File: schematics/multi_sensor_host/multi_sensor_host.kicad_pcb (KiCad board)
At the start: 2 copper layers, 70 x 146 mm, 173 parts, among them J1 left hand 0, J10 swd, J11 stm_boot, J13 right hand 0, J14 right hand 1, J15 right hand 2, J16 right hand 3, J17 rst, J18 left hand 3, J19 left leg 0, J2 left hand 1, J20 left leg 1, J21 right lef 0, J22 right leg 1, J23 torso 0, J24 torso 1, J25 torso 2, J26 torso 3, J3 bm_cfg, J4 left hand 2, J5 tx, J6 MY_USB_B, J8 rx, J9 uart1, U1 TCA9548A_TSSOP, U11 MCP111, U12 BM71BLES1FC2-0B02AA, U2 TCA9548A_TSSOP, U3 74HC165, U4 74HC165, U5 74HC165, U6 74HC165, U8 MCP73812, U9 MCP1603, Y1 Crystal

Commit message: Probably good enough...
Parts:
- moved J9 0.11 mm to (72.1, 129.1)
- moved C31 0.10 mm to (71.9, 124.4)
- moved R93 0.10 mm to (74.9, 130.4)
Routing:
- net VDD: track 1108.4 -> 1096.4 mm
- net /rst: track 153.4 -> 155.3 mm
- net /stm_rx: track 78.6 -> 79.5 mm
- net /stm_tx: track 86.3 -> 87.2 mm

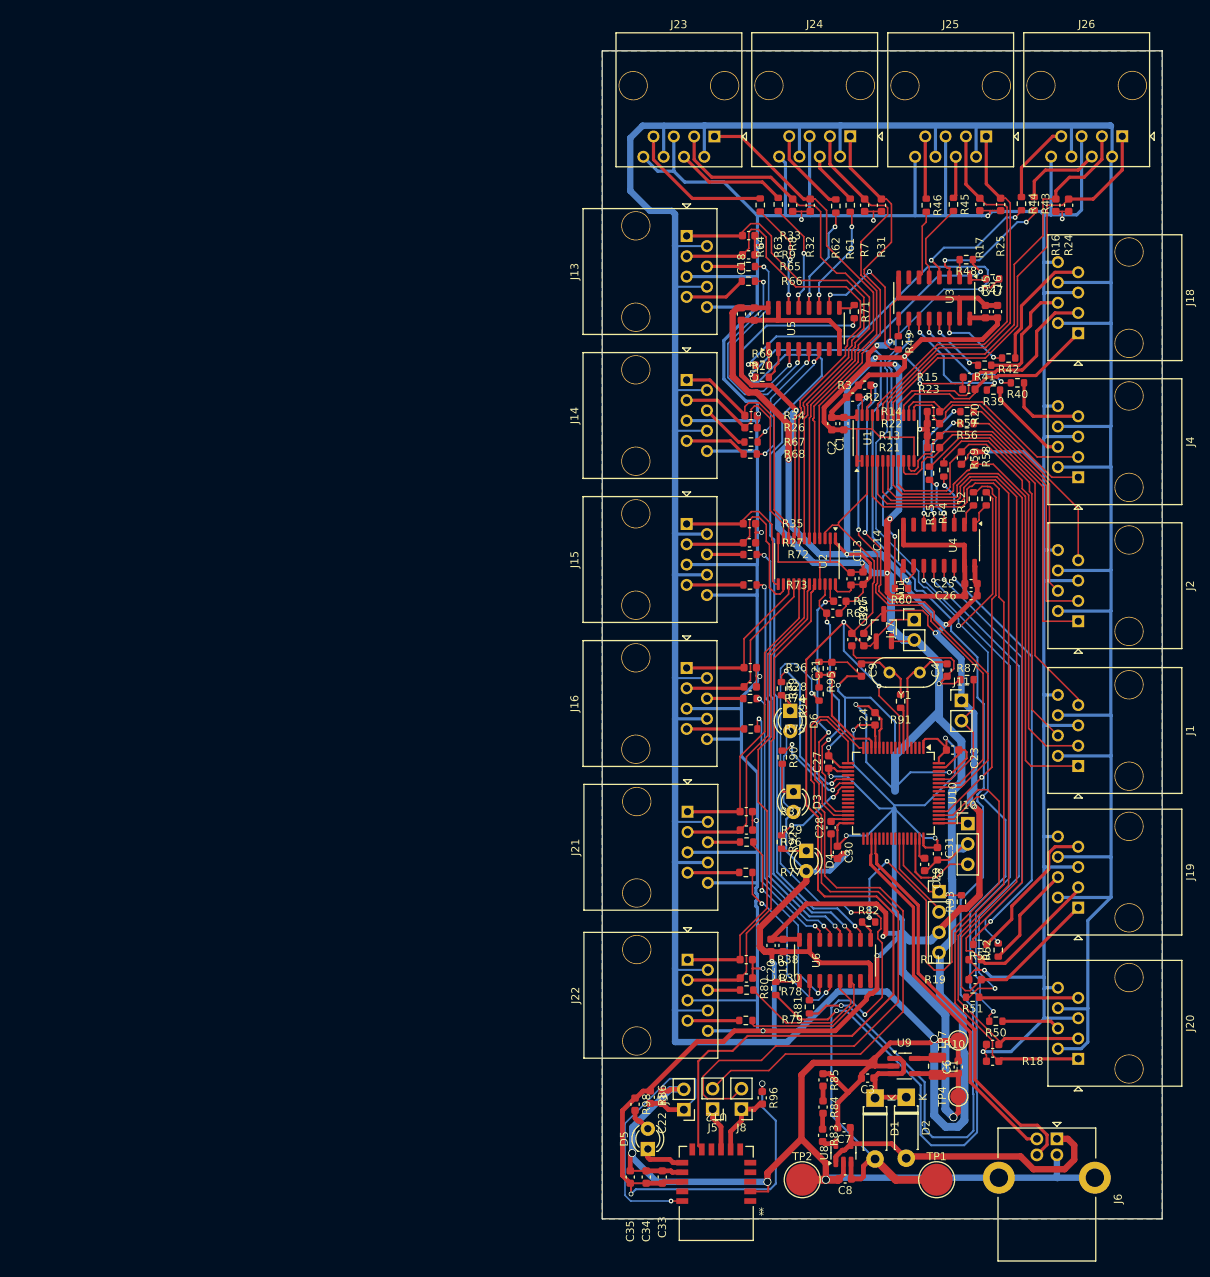
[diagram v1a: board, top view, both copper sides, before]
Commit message: Removing old wires.
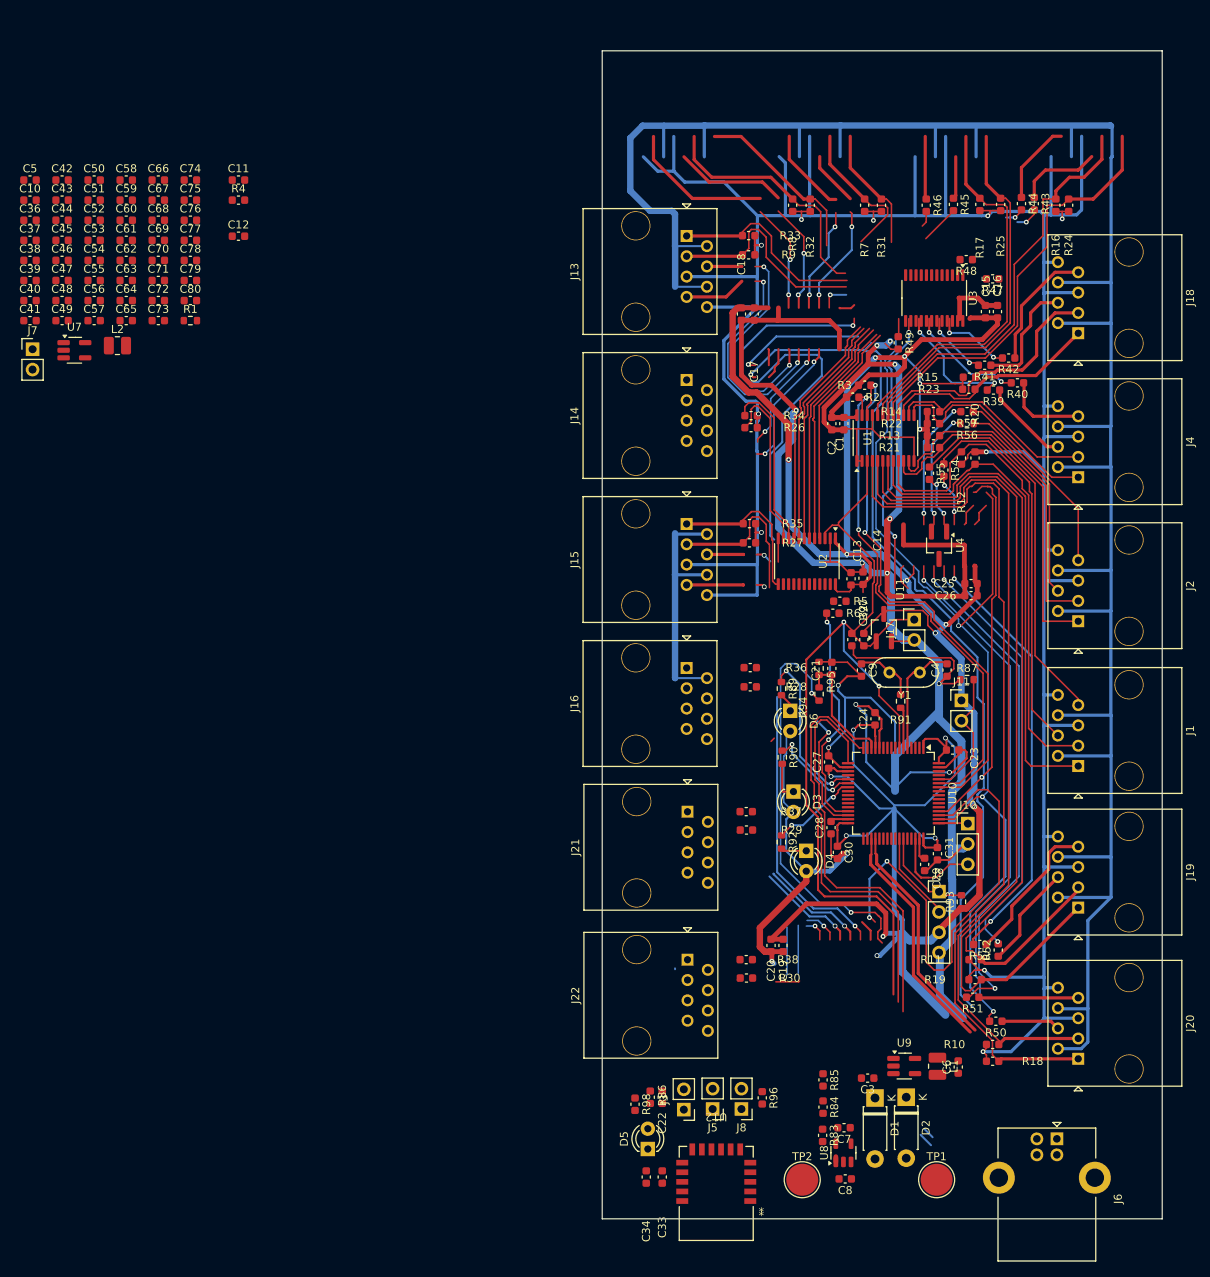
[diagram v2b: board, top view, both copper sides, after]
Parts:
- removed C35: 4u7, Capacitor_SMD:C_0603_1608Metric
- removed J23: torso 0, Connector_RJ:RJ45_OST_PJ012-8P8CX_Vertical
- removed J24: torso 1, Connector_RJ:RJ45_OST_PJ012-8P8CX_Vertical
- removed J25: torso 2, Connector_RJ:RJ45_OST_PJ012-8P8CX_Vertical
- removed J26: torso 3, Connector_RJ:RJ45_OST_PJ012-8P8CX_Vertical
- removed R58, R59, R60, R61, R62, R63, R64, R65, R66, R67, R68, R69, R70, R71, R72, R73, R74, R75, R76, R77, R78, R79, R80, R81, R82: 2k, Resistor_SMD:R_0603_1608Metric
- removed TP4: Vdd, TestPoint:TestPoint_Pad_D2.0mm
- removed TP7: gnd, TestPoint:TestPoint_Pad_D2.0mm
- removed U5, U6: 74HC165, Package_SO:SO-16_3.9x9.9mm_P1.27mm
- added C10: 22u, Capacitor_SMD:C_0603_1608Metric, F.Cu at (-41.5, 42.7)
- added C11: 100n, Capacitor_SMD:C_0603_1608Metric, F.Cu at (-15.5, 40.1)
- added C12: 22u, Capacitor_SMD:C_0603_1608Metric, F.Cu at (-15.5, 47.2)
- added C36: 4u7, Capacitor_SMD:C_0603_1608Metric, F.Cu at (-41.5, 45.2)
- added C37: 100n, Capacitor_SMD:C_0603_1608Metric, F.Cu at (-41.5, 47.7)
- added C38: 4u7, Capacitor_SMD:C_0603_1608Metric, F.Cu at (-41.5, 50.2)
- added C39: 100n, Capacitor_SMD:C_0603_1608Metric, F.Cu at (-41.5, 52.7)
- added C40: 4u7, Capacitor_SMD:C_0603_1608Metric, F.Cu at (-41.5, 55.2)
- added C41: 100n, Capacitor_SMD:C_0603_1608Metric, F.Cu at (-41.5, 57.7)
- added C42: 4u7, Capacitor_SMD:C_0603_1608Metric, F.Cu at (-37.5, 40.1)
- added C43: 100n, Capacitor_SMD:C_0603_1608Metric, F.Cu at (-37.5, 42.7)
- added C44: 4u7, Capacitor_SMD:C_0603_1608Metric, F.Cu at (-37.5, 45.2)
- added C45: 100n, Capacitor_SMD:C_0603_1608Metric, F.Cu at (-37.5, 47.7)
- added C46: 4u7, Capacitor_SMD:C_0603_1608Metric, F.Cu at (-37.5, 50.2)
- added C47: 100n, Capacitor_SMD:C_0603_1608Metric, F.Cu at (-37.5, 52.7)
- added C48: 4u7, Capacitor_SMD:C_0603_1608Metric, F.Cu at (-37.5, 55.2)
- added C49: 100n, Capacitor_SMD:C_0603_1608Metric, F.Cu at (-37.5, 57.7)
- added C5: 4u7, Capacitor_SMD:C_0603_1608Metric, F.Cu at (-41.5, 40.1)
- added C50: 4u7, Capacitor_SMD:C_0603_1608Metric, F.Cu at (-33.5, 40.1)
- added C51: 100n, Capacitor_SMD:C_0603_1608Metric, F.Cu at (-33.5, 42.7)
- added C52: 4u7, Capacitor_SMD:C_0603_1608Metric, F.Cu at (-33.5, 45.2)
- added C53: 100n, Capacitor_SMD:C_0603_1608Metric, F.Cu at (-33.5, 47.7)
- added C54: 4u7, Capacitor_SMD:C_0603_1608Metric, F.Cu at (-33.5, 50.2)
- added C55: 100n, Capacitor_SMD:C_0603_1608Metric, F.Cu at (-33.5, 52.7)
- added C56: 4u7, Capacitor_SMD:C_0603_1608Metric, F.Cu at (-33.5, 55.2)
- added C57: 100n, Capacitor_SMD:C_0603_1608Metric, F.Cu at (-33.5, 57.7)
- added C58: 4u7, Capacitor_SMD:C_0603_1608Metric, F.Cu at (-29.5, 40.1)
- added C59: 100n, Capacitor_SMD:C_0603_1608Metric, F.Cu at (-29.5, 42.7)
- added C60: 4u7, Capacitor_SMD:C_0603_1608Metric, F.Cu at (-29.5, 45.2)
- added C61: 100n, Capacitor_SMD:C_0603_1608Metric, F.Cu at (-29.5, 47.7)
- added C62: 4u7, Capacitor_SMD:C_0603_1608Metric, F.Cu at (-29.5, 50.2)
- added C63: 100n, Capacitor_SMD:C_0603_1608Metric, F.Cu at (-29.5, 52.7)
- added C64: 4u7, Capacitor_SMD:C_0603_1608Metric, F.Cu at (-29.5, 55.2)
- added C65: 100n, Capacitor_SMD:C_0603_1608Metric, F.Cu at (-29.5, 57.7)
- added C66: 4u7, Capacitor_SMD:C_0603_1608Metric, F.Cu at (-25.5, 40.1)
- added C67: 100n, Capacitor_SMD:C_0603_1608Metric, F.Cu at (-25.5, 42.7)
- added C68: 4u7, Capacitor_SMD:C_0603_1608Metric, F.Cu at (-25.5, 45.2)
- added C69: 100n, Capacitor_SMD:C_0603_1608Metric, F.Cu at (-25.5, 47.7)
- added C70: 4u7, Capacitor_SMD:C_0603_1608Metric, F.Cu at (-25.5, 50.2)
- added C71: 100n, Capacitor_SMD:C_0603_1608Metric, F.Cu at (-25.5, 52.7)
- added C72: 4u7, Capacitor_SMD:C_0603_1608Metric, F.Cu at (-25.5, 55.2)
- added C73: 100n, Capacitor_SMD:C_0603_1608Metric, F.Cu at (-25.5, 57.7)
- added C74: 4u7, Capacitor_SMD:C_0603_1608Metric, F.Cu at (-21.5, 40.1)
- added C75: 100n, Capacitor_SMD:C_0603_1608Metric, F.Cu at (-21.5, 42.7)
- added C76: 4u7, Capacitor_SMD:C_0603_1608Metric, F.Cu at (-21.5, 45.2)
- added C77: 100n, Capacitor_SMD:C_0603_1608Metric, F.Cu at (-21.5, 47.7)
- added C78: 4u7, Capacitor_SMD:C_0603_1608Metric, F.Cu at (-21.5, 50.2)
- added C79: 100n, Capacitor_SMD:C_0603_1608Metric, F.Cu at (-21.5, 52.7)
- added C80: 22u, Capacitor_SMD:C_0603_1608Metric, F.Cu at (-21.5, 55.2)
- added J7: rst_bm71, Connector_PinHeader_2.54mm:PinHeader_1x02_P2.54mm_Vertical, F.Cu at (-41.2, 61.3)
- added L2: 4.7uH, Inductor_SMD:L_1008_2520Metric, F.Cu at (-30.6, 60.9)
- added R1: 100k, Resistor_SMD:R_0603_1608Metric, F.Cu at (-21.5, 57.7)
- added R4: 2k, Capacitor_SMD:C_0603_1608Metric, F.Cu at (-15.5, 42.7)
- added U7: MCP1603, Package_TO_SOT_SMD:SOT-23-5_HandSoldering, F.Cu at (-36.0, 61.4)
- C14, C2, C33, C34, C6: value 4u7 -> 22u
- C15, C19, C25: value 100n -> 4u7
- C16, C18, C20, C26: value 4u7 -> 100n
- J17: value rst -> rst_mcu
- R39, R40, R41, R42, R43, R44, R45, R46, R47, R48, R49, R50, R51, R52, R53, R54, R55: footprint Resistor_SMD:R_0603_1608Metric -> Capacitor_SMD:C_0603_1608Metric
- R56: value 2k -> 100k
- R57: value 2k -> 10k; footprint Resistor_SMD:R_0603_1608Metric -> Capacitor_SMD:C_0603_1608Metric
- U3: value 74HC165 -> TCA9548A_TSSOP; footprint Package_SO:SO-16_3.9x9.9mm_P1.27mm -> Package_SO:TSSOP-24_4.4x7.8mm_P0.65mm
- U4: value 74HC165 -> MCP111; footprint Package_SO:SO-16_3.9x9.9mm_P1.27mm -> Package_TO_SOT_SMD:TSOT-23_HandSoldering
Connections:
- net /lh_scl_2 renamed /scl_4
- net /lh_sda_2 renamed /sda_4
- net /rh_scl_2 renamed /scl_12
- net /rh_sda_2 renamed /sda_12
- C15 pad 1: VDD -> /rst_bm71
- C16 pad 1: VDD -> VCC
- C18 pad 1: VDD -> VCC
- C32 pad 1: /rst -> /rst_mcu
- C33 pad 1: VDD -> VCC
- C34 pad 1: VDD -> VCC
- J1 pad 1: /lh_sda_0 -> /sda_0
- J1 pad 3: /lh_scl_0 -> /scl_0
- J1 pad 4: /lh_int_0_0 -> /sda_1
- J1 pad 7: /lh_int_0_1 -> /scl_1
- J13 pad 1: /rh_sda_0 -> /sda_8
- J13 pad 3: /rh_scl_0 -> /scl_8
- J13 pad 4: /rh_int_0_0 -> /sda_9
- J13 pad 7: /rh_int_0_1 -> /scl_9
- J14 pad 1: /rh_sda_1 -> /sda_10
- J14 pad 3: /rh_scl_1 -> /scl_10
- J14 pad 4: /rh_int_1_0 -> /sda_11
- J14 pad 7: /rh_int_1_1 -> /scl_11
- J15 pad 4: /rh_int_2_0 -> /sda_13
- J15 pad 7: /rh_int_2_1 -> /scl_13
- J16 pad 1: /rh_sda_3 -> /sda_14
- J16 pad 3: /rh_scl_3 -> /scl_14
- J16 pad 4: /rh_int_3_0 -> /sda_15
- J16 pad 7: /rh_int_3_1 -> /scl_15
- J17 pad 1: /rst -> /rst_mcu
- J18 pad 1: /lh_sda_3 -> /sda_6
- J18 pad 3: /lh_scl_3 -> /scl_6
- J18 pad 4: /lh_int_3_0 -> /sda_7
- J18 pad 7: /lh_int_3_1 -> /scl_7
- J19 pad 1: /ll_sda_0 -> /sda_16
- J19 pad 3: /ll_scl_0 -> /scl_16
- J19 pad 4: /ll_int_0_0 -> /sda_17
- J19 pad 7: /ll_int_0_1 -> /scl_17
- J2 pad 1: /lh_sda_1 -> /sda_2
- J2 pad 3: /lh_scl_1 -> /scl_2
- J2 pad 4: /lh_int_1_0 -> /sda_3
- J2 pad 7: /lh_int_1_1 -> /scl_3
- J20 pad 1: /ll_sda_1 -> /sda_18
- J20 pad 3: /ll_scl_1 -> /scl_18
- J20 pad 4: /ll_int_1_0 -> /sda_19
- J20 pad 7: /ll_int_1_1 -> /scl_19
- J21 pad 1: /rl_sda_0 -> /sda_20
- J21 pad 3: /rl_scl_0 -> /scl_20
- J21 pad 4: /rl_int_0_0 -> /sda_21
- J21 pad 7: /rl_int_0_1 -> /scl_21
- J22 pad 1: /rl_sda_1 -> /sda_22
- J22 pad 3: /rl_scl_1 -> /scl_22
- J22 pad 4: /rl_int_1_0 -> /sda_23
- J22 pad 7: /rl_int_1_1 -> /scl_23
- J4 pad 4: /lh_int_2_0 -> /sda_5
- J4 pad 7: /lh_int_2_1 -> /scl_5
- R10 pad 2: /ll_scl_1 -> /scl_0
- R11 pad 2: /ll_scl_0 -> /scl_1
- R12 pad 2: /lh_scl_0 -> /scl_2
- R13 pad 2: /lh_scl_1 -> /scl_3
- R15 pad 2: /lh_scl_3 -> /scl_5
- R16 pad 2: /t_scl_3 -> /scl_6
- R17 pad 2: /t_scl_2 -> /scl_7
- R18 pad 2: /ll_sda_1 -> /sda_0
- R19 pad 2: /ll_sda_0 -> /sda_1
- R20 pad 2: /lh_sda_0 -> /sda_2
- R21 pad 2: /lh_sda_1 -> /sda_3
- R23 pad 2: /lh_sda_3 -> /sda_5
- R24 pad 2: /t_sda_3 -> /sda_6
- R25 pad 2: /t_sda_2 -> /sda_7
- R26 pad 2: /rh_scl_1 -> /scl_11
- R28 pad 2: /rh_scl_3 -> /scl_13
- R29 pad 2: /rl_scl_0 -> /scl_14
- R30 pad 2: /rl_scl_1 -> /scl_15
- R31 pad 2: /t_sda_1 -> /sda_8
- R32 pad 2: /t_sda_0 -> /sda_9
- R33 pad 2: /rh_sda_0 -> /sda_10
- R34 pad 2: /rh_sda_1 -> /sda_11
- R36 pad 2: /rh_sda_3 -> /sda_13
- R37 pad 2: /rl_sda_0 -> /sda_14
- R38 pad 2: /rl_sda_1 -> /sda_15
- R39 pad 1: /lh_int_2_0 -> VDD
- R39 pad 2: Net-(U3-D0) -> /scl_host_c
- R40 pad 1: /lh_int_2_1 -> VDD
- R40 pad 2: Net-(U3-D1) -> /scl_16
- R41 pad 1: /lh_int_3_0 -> VDD
- R41 pad 2: Net-(U3-D2) -> /scl_17
- R42 pad 1: /lh_int_3_1 -> VDD
- R42 pad 2: Net-(U3-D3) -> /scl_18
- R43 pad 1: /t_int_3_0 -> VDD
- R43 pad 2: Net-(U3-D4) -> /scl_19
- R44 pad 1: /t_int_3_1 -> VDD
- R44 pad 2: Net-(U3-D5) -> /scl_20
- R45 pad 1: /t_int_2_0 -> VDD
- R45 pad 2: Net-(U3-D6) -> /scl_21
- R46 pad 1: /t_int_2_1 -> VDD
- R46 pad 2: Net-(U3-D7) -> /scl_22
- R47 pad 1: /parallel_load -> VDD
- R47 pad 2: Net-(U3-~{PL}) -> /scl_23
- R48 pad 1: /shifter_clock -> VDD
- R48 pad 2: Net-(U3-CP) -> /sda_16
- R49 pad 1: Net-(U3-Q7) -> VDD
- R49 pad 2: /parallel_input_sheet1/serial_output -> /sda_17
- R50 pad 1: /ll_int_1_0 -> VDD
- R50 pad 2: Net-(U4-D0) -> /sda_18
- R51 pad 1: /ll_int_1_1 -> VDD
- R51 pad 2: Net-(U4-D1) -> /sda_19
- R52 pad 1: /ll_int_0_0 -> VDD
- R52 pad 2: Net-(U4-D2) -> /sda_20
- R53 pad 1: /ll_int_0_1 -> VDD
- R53 pad 2: Net-(U4-D3) -> /sda_21
- R54 pad 1: /lh_int_0_0 -> VDD
- R54 pad 2: Net-(U4-D4) -> /sda_22
- R55 pad 1: /lh_int_0_1 -> VDD
- R55 pad 2: Net-(U4-D5) -> /sda_23
- R56 pad 1: /lh_int_1_0 -> /batt_charge_en
- R56 pad 2: Net-(U4-D6) -> GND
- R57 pad 1: /lh_int_1_1 -> VCC
- R57 pad 2: Net-(U4-D7) -> /rst_bm71
- R7 pad 2: /t_scl_1 -> /scl_8
- R8 pad 2: /t_scl_0 -> /scl_9
- R86 pad 1: VDD -> VCC
- R9 pad 2: /rh_scl_0 -> /scl_10
- R96 pad 1: VDD -> VCC
- R97 pad 2: /rst -> /rst_mcu
- R98 pad 1: VDD -> VCC
- U1 pad 10: /lh_sda_1 -> /sda_3
- U1 pad 11: /lh_scl_1 -> /scl_3
- U1 pad 15: /lh_sda_3 -> /sda_5
- U1 pad 16: /lh_scl_3 -> /scl_5
- U1 pad 17: /t_sda_3 -> /sda_6
- U1 pad 18: /t_scl_3 -> /scl_6
- U1 pad 19: /t_sda_2 -> /sda_7
- U1 pad 20: /t_scl_2 -> /scl_7
- U1 pad 3: /rst -> /rst_mcu
- U1 pad 4: /ll_sda_1 -> /sda_0
- U1 pad 5: /ll_scl_1 -> /scl_0
- U1 pad 6: /ll_sda_0 -> /sda_1
- U1 pad 7: /ll_scl_0 -> /scl_1
- U1 pad 8: /lh_sda_0 -> /sda_2
- U1 pad 9: /lh_scl_0 -> /scl_2
- U10 pad 15: unconnected-(U10A-PA1-Pad15) -> /batt_charge_en
- U10 pad 28: unconnected-(U10A-PB2-Pad28) -> /boot1
- U10 pad 35: /usb_d- -> unconnected-(U10A-PB14___OTG_HS_DM-Pad35)
- U10 pad 36: /usb_d+ -> unconnected-(U10A-PB15___OTG_HS_DP-Pad36)
- U10 pad 40: unconnected-(U10A-PC9-Pad40) -> /sda_host_c
- U10 pad 41: unconnected-(U10A-PA8__OTG_FS_SOF-Pad41) -> /scl_host_c
- U10 pad 44: unconnected-(U10A-PA11___OTG_FS_DM-Pad44) -> /usb_d-
- U10 pad 45: unconnected-(U10A-PA12___OTG_FS_DP-Pad45) -> /usb_d+
- U10 pad 50: /parallel_load -> unconnected-(U10A-PA15___JTDI-Pad50)
- U10 pad 51: /data_serial -> unconnected-(U10A-PC10___USART4_TX-Pad51)
- U10 pad 52: /shifter_clock -> unconnected-(U10A-PC11__USART4_RX-Pad52)
- U10 pad 7: /rst -> /rst_mcu
- U11 pad 1: /rst -> /rst_mcu
- U12 pad 10: /rst -> /rst_bm71
- U12 pad 14: VDD -> VCC
- U2 pad 1: VDD -> GND
- U2 pad 10: /rh_sda_1 -> /sda_11
- U2 pad 11: /rh_scl_1 -> /scl_11
- U2 pad 15: /rh_sda_3 -> /sda_13
- U2 pad 16: /rh_scl_3 -> /scl_13
- U2 pad 17: /rl_sda_0 -> /sda_14
- U2 pad 18: /rl_scl_0 -> /scl_14
- U2 pad 19: /rl_sda_1 -> /sda_15
- U2 pad 20: /rl_scl_1 -> /scl_15
- U2 pad 3: /rst -> /rst_mcu
- U2 pad 4: /t_sda_1 -> /sda_8
- U2 pad 5: /t_scl_1 -> /scl_8
- U2 pad 6: /t_sda_0 -> /sda_9
- U2 pad 7: /t_scl_0 -> /scl_9
- U2 pad 8: /rh_sda_0 -> /sda_10
- U2 pad 9: /rh_scl_0 -> /scl_10
- U3 pad 1: Net-(U3-~{PL}) -> GND
- U3 pad 10: /parallel_input_sheet/serial_output -> /sda_19
- U3 pad 11: Net-(U3-D0) -> /scl_19
- U3 pad 12: Net-(U3-D1) -> GND
- U3 pad 13: Net-(U3-D2) -> /sda_20
- U3 pad 14: Net-(U3-D3) -> /scl_20
- U3 pad 15: GND -> /sda_21
- U3 pad 16: VDD -> /scl_21
- U3 pad 2: Net-(U3-CP) -> GND
- U3 pad 3: Net-(U3-D4) -> /rst_mcu
- U3 pad 4: Net-(U3-D5) -> /sda_16
- U3 pad 5: Net-(U3-D6) -> /scl_16
- U3 pad 6: Net-(U3-D7) -> /sda_17
- U3 pad 7: unconnected-(U3-~{Q7}-Pad7) -> /scl_17
- U3 pad 8: GND -> /sda_18
- U3 pad 9: Net-(U3-Q7) -> /scl_18
- U4 pad 1: Net-(U4-~{PL}) -> /rst_bm71
- U4 pad 2: Net-(U4-CP) -> GND
- U4 pad 3: Net-(U4-D4) -> VCC
- U8 pad 1: /Vbus -> /batt_charge_en
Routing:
- net (no net): track 0.00 -> 1433.7 mm, vias 0 -> 35
- net GND: track 1243.5 -> 842.5 mm, vias 18 -> 16
- net VDD: track 1096.4 -> 867.1 mm, vias 34 -> 27
- net /parallel_load: track 229.0 -> 0.00 mm, vias 5 -> 0
- net /shifter_clock: track 223.5 -> 0.00 mm, vias 4 -> 0
- net unconnected-(U10A-PC11__USART4_RX-Pad52): track 0.00 -> 157.2 mm, vias 0 -> 2
- net /rst: track 155.3 -> 0.00 mm, vias 2 -> 0
- net unconnected-(U10A-PA15___JTDI-Pad50): track 0.00 -> 118.7 mm, vias 0 -> 2
- net /rst_mcu: track 0.00 -> 116.2 mm, vias 0 -> 2
- net /parallel_input_sheet2/serial_output: track 113.1 -> 0.00 mm, vias 2 -> 0
- net /ll_sda_1: track 109.9 -> 0.00 mm
- net /ll_scl_1: track 107.6 -> 0.00 mm
- net /ll_sda_0: track 107.3 -> 0.00 mm
- net /ll_scl_0: track 102.3 -> 0.00 mm
- net /t_scl_0: track 68.9 -> 0.00 mm
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- removed copper zone on B.Cu, net GND
- removed copper zone on F.Cu, net GND

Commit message: Upgraded to KiCad9.0.
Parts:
- moved J1 185.3 mm to (31.7, -62.6), turned to 180 degrees
- moved J2 175.4 mm to (13.2, -62.6), turned to 180 degrees
- moved J4 141.5 mm to (68.6, -62.6), turned to 180 degrees
- moved J18 128.2 mm to (50.1, -62.6), turned to 180 degrees
- moved U1 114.3 mm to (36.3, -38.2), turned to -90 degrees
- moved C1 108.2 mm to (41.8, -36.0), turned to 90 degrees
- moved C2 107.7 mm to (43.5, -36.0), turned to 90 degrees
- moved R2 101.3 mm to (40.2, -31.7), turned to 90 degrees
- moved R3 100.5 mm to (38.6, -31.7), turned to 90 degrees
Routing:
- net (no net): track 1433.7 -> 0.00 mm, vias 35 -> 0
- net VDD: track 867.1 -> 0.00 mm, vias 27 -> 0
- net GND: track 842.5 -> 0.00 mm, vias 16 -> 0
- net unconnected-(U10A-PC11__USART4_RX-Pad52): track 157.2 -> 0.00 mm, vias 2 -> 0
- net unconnected-(U10A-PA15___JTDI-Pad50): track 118.7 -> 0.00 mm, vias 2 -> 0
- net /rst_mcu: track 116.2 -> 0.00 mm, vias 2 -> 0
- net /scl_host_a: track 68.6 -> 0.00 mm, vias 2 -> 0
- net /scl_9: track 68.5 -> 0.00 mm
- net /sda_host_a: track 64.8 -> 0.00 mm, vias 2 -> 0
- net /sda_18: track 64.4 -> 0.00 mm, vias 2 -> 0
- net /sda_19: track 64.3 -> 0.00 mm, vias 2 -> 0
- net unconnected-(U10A-PC10___USART4_TX-Pad51): track 59.6 -> 0.00 mm, vias 2 -> 0
- net /sda_9: track 56.0 -> 0.00 mm
- net /sda_21: track 54.4 -> 0.00 mm, vias 2 -> 0
- net /sda_20: track 53.8 -> 0.00 mm, vias 2 -> 0
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
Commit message: Replaced buck with low drop linear for the bluetooth.
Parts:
- removed C25, C38, C42, C46, C50, C54, C58, C62, C66, C70, C74, C78: 4u7, Capacitor_SMD:C_0603_1608Metric
- removed C26, C39, C43, C47, C51, C55, C59, C63, C67, C71, C75, C79: 100n, Capacitor_SMD:C_0603_1608Metric
- removed L2: 4.7uH, Inductor_SMD:L_1008_2520Metric
- removed U7: MCP1603, Package_TO_SOT_SMD:SOT-23-5_HandSoldering
- added C35: 10n, Capacitor_SMD:C_0603_1608Metric, F.Cu at (-18.8, 26.0)
- added U5: TPS79333-EP, Package_TO_SOT_SMD:SOT-23-5, F.Cu at (-18.2, 22.5)
- moved J21 310.5 mm to (293.2, -61.6), turned to 180 degrees
- moved J22 307.3 mm to (274.7, -61.6), turned to 180 degrees
- moved C11 288.5 mm to (263.0, -35.3), turned to 90 degrees
- moved R4 286.7 mm to (261.5, -31.3), turned to 90 degrees
- moved J20 258.4 mm to (237.7, -61.6), turned to 180 degrees
- moved J19 254.8 mm to (256.2, -61.6), turned to 180 degrees
- moved C14 238.0 mm to (265.0, -35.3)
- moved U3 207.5 mm to (257.0, -38.0)
- moved R39 205.3 mm to (259.5, -31.3), turned to 90 degrees
- moved J16 199.7 mm to (156.2, -61.6), turned to 180 degrees
- moved J15 197.4 mm to (174.7, -61.6), turned to 180 degrees
- moved C19 196.7 mm to (2.00, -54.2)
- moved C20 195.8 mm to (4.00, -54.2)
- moved C12 178.0 mm to (142.0, -35.8), turned to 90 degrees
- moved J14 149.2 mm to (119.2, -61.6), turned to 180 degrees
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
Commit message: Groupping different logical component groups to move them together.
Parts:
- TP1, TP2: footprint TestPoint:TestPoint_Pad_D4.0mm -> Connector_PinHeader_1.00mm:PinHeader_1x01_P1.00mm_Vertical
- moved U5 231.9 mm to (50.3, 244.0)
- moved C35 231.5 mm to (50.2, 247.0), turned to 180 degrees
- moved C5 222.5 mm to (47.0, 244.2), turned to 90 degrees
- moved C80 203.3 mm to (53.5, 244.2), turned to -90 degrees
- moved C15 199.5 mm to (1.73, 241.0), turned to 180 degrees
- moved R56 197.4 mm to (51.2, 266.5), turned to 0 degrees
- moved J7 191.9 mm to (5.04, 247.5), turned to -90 degrees
- moved C18 187.5 mm to (55.5, 244.2)
- moved R57 185.7 mm to (5.28, 241.0)
- moved C17 174.3 mm to (61.0, 230.8), turned to 90 degrees
- moved U4 172.3 mm to (3.79, 244.0), turned to 0 degrees
- moved J17 152.0 mm to (4.00, 232.5), turned to -90 degrees
- moved U11 146.5 mm to (3.00, 228.7), turned to 0 degrees
- moved C32 141.2 mm to (1.32, 225.5), turned to 180 degrees
- moved R97 140.4 mm to (4.83, 225.5), turned to 180 degrees
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
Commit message: a
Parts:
- moved C16 218.7 mm to (-31.8, 244.9)
- moved C10 197.7 mm to (-33.5, 240.2)
- moved C33 107.2 mm to (-33.8, 244.9)
- moved J5 106.4 mm to (-24.8, 237.7)
- moved U12 106.3 mm to (-25.5, 247.0)
- moved J8 106.2 mm to (-20.8, 237.7)
- moved R96 104.9 mm to (-17.8, 234.9)
- moved C34 103.7 mm to (-33.5, 242.2), turned to 0 degrees
- moved D5 102.0 mm to (-32.7, 237.0)
- moved R98 101.0 mm to (-32.8, 231.4)
- moved R86 100.4 mm to (-29.8, 230.7), turned to 90 degrees
- moved J3 99.9 mm to (-27.1, 230.2)
- moved C22 99.0 mm to (-29.8, 227.4)

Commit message: a
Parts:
- moved R18 210.2 mm to (31.8, -54.2), turned to -90 degrees
- moved R10 208.7 mm to (29.5, -54.2), turned to 90 degrees
- moved R19 200.5 mm to (27.4, -54.2), turned to 90 degrees
- moved R11 198.9 mm to (24.0, -54.2), turned to 90 degrees
- moved R26 167.3 mm to (-102.8, -0.20)
- moved R27 167.3 mm to (-103.0, 14.2)
- moved R31 167.3 mm to (-86.5, -28.0)
- moved R32 167.3 mm to (-95.4, -28.0)
- moved R34 167.3 mm to (-102.8, -1.70)
- moved R35 167.3 mm to (-103.0, 11.8)
- moved R40 167.3 mm to (-69.5, -5.80)
- moved R43 167.3 mm to (-67.4, -28.2)
- moved R44 167.3 mm to (-69.0, -28.2)
- moved R45 167.3 mm to (-77.5, -28.1)
- moved R46 167.3 mm to (-80.9, -28.0)
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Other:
- board outline removed
